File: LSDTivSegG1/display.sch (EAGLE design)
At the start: 99 parts, among them IC1 MEGA8-P, IC2 MAX232, IC3 PCF8574P, IC4 PCF8574P, IC5 PCF8574P, IC6 PCF8574P

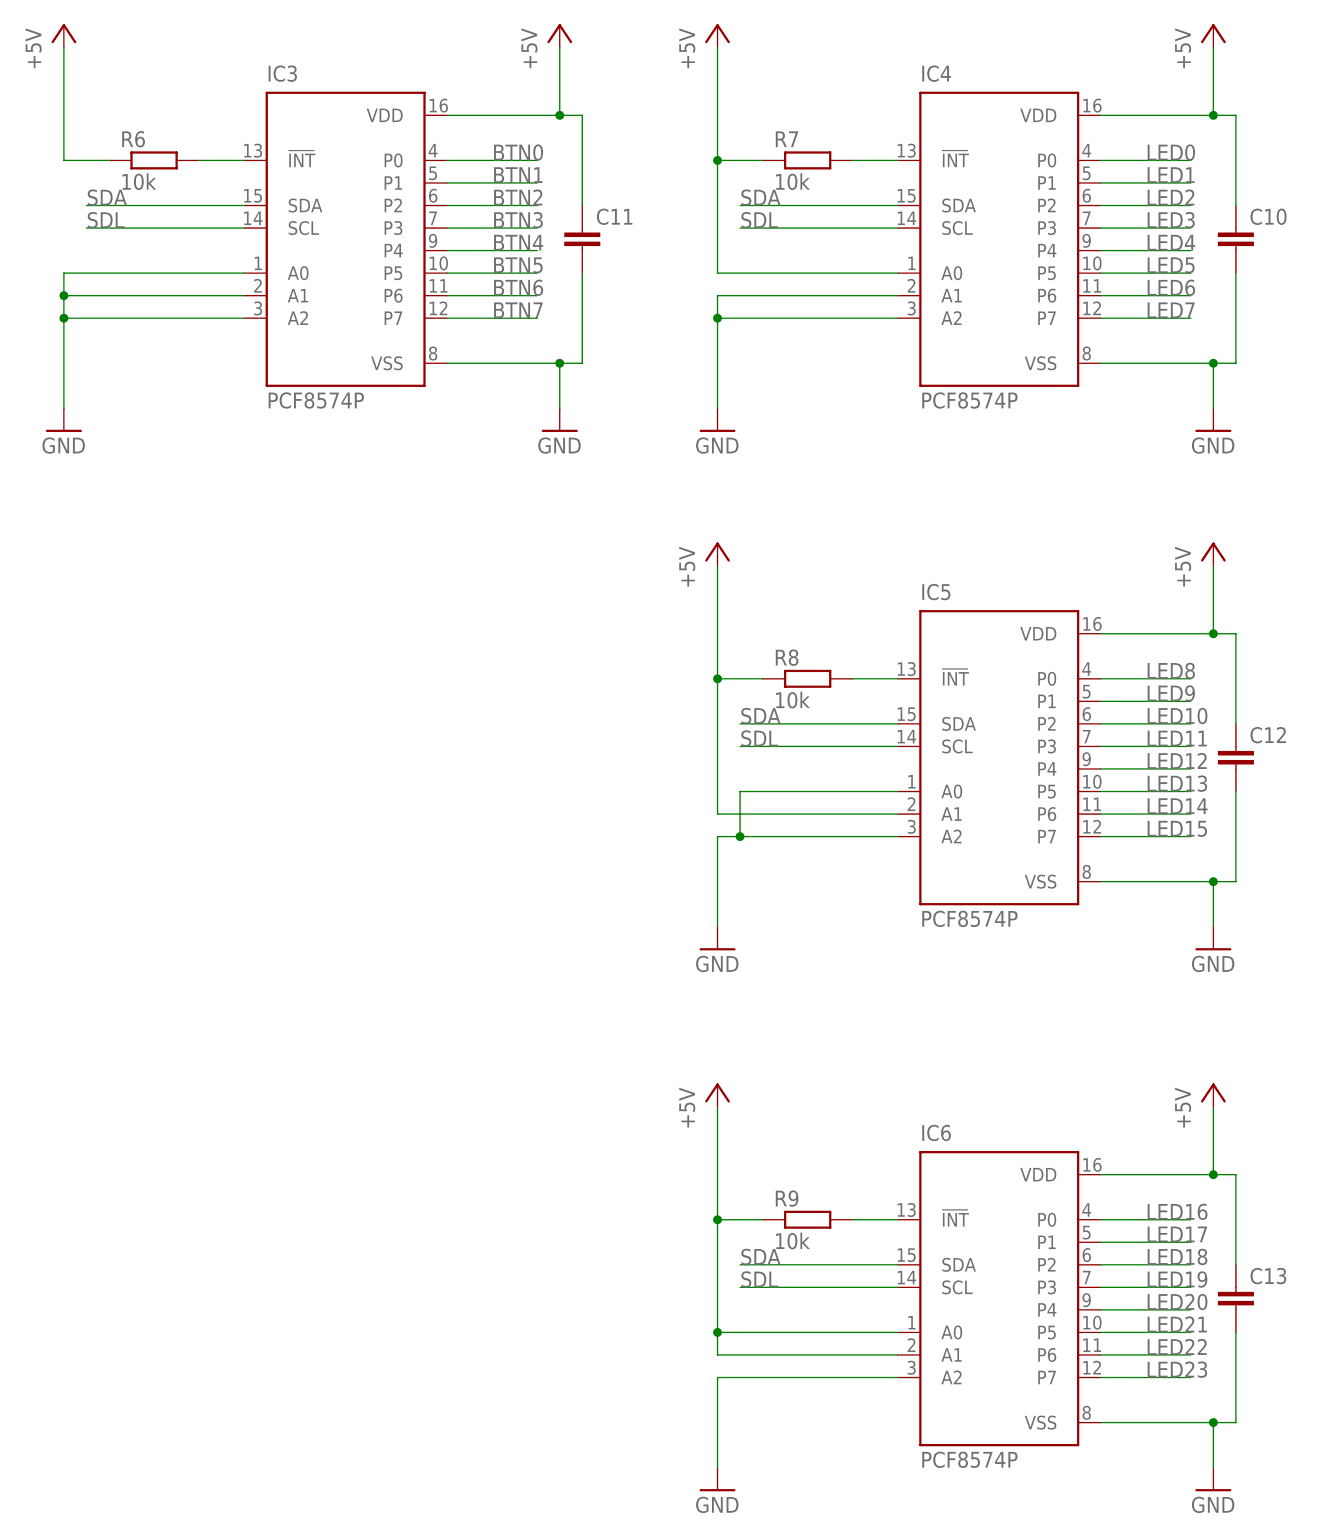
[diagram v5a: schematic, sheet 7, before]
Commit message: added values to PCF blocking capacities
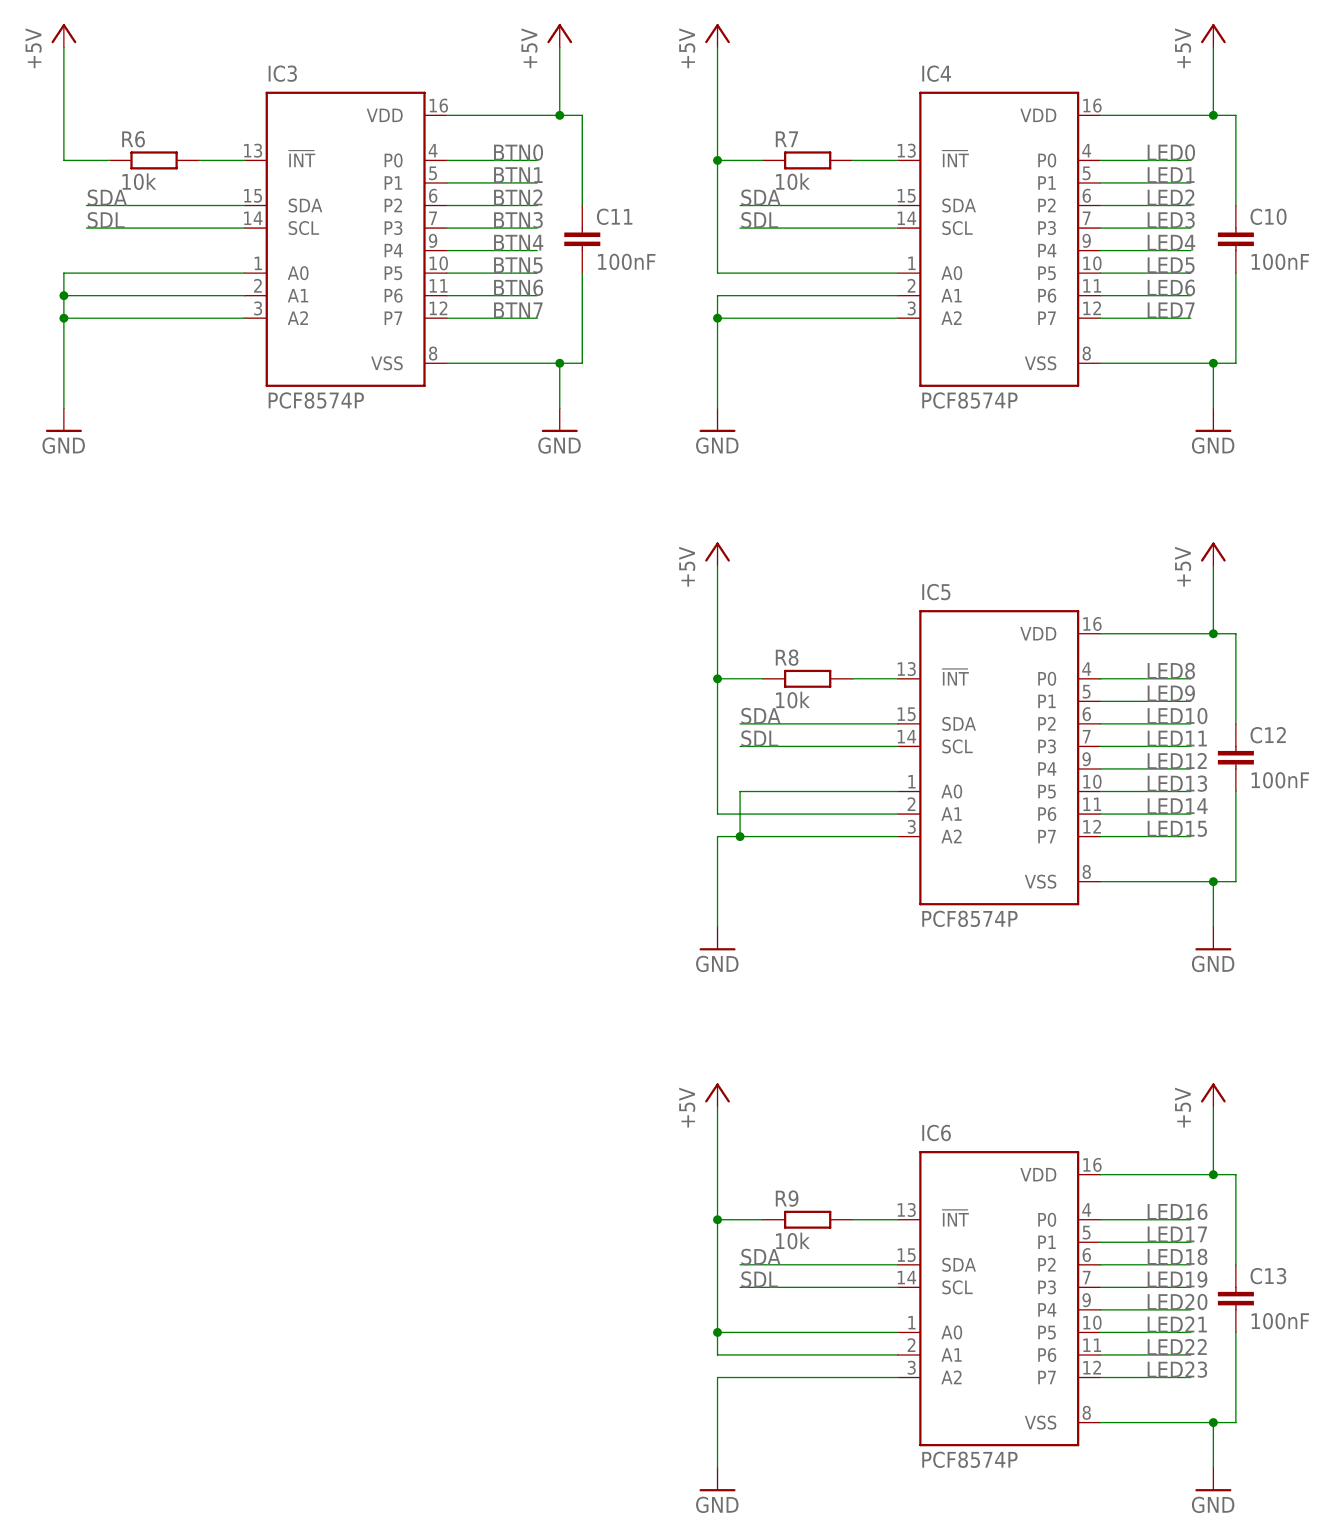
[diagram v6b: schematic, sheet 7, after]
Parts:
- C10, C11, C12, C13: value (none) -> 100nF
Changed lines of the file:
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@@
 <part name="JP1" library="pinhead" library_urn="urn:adsk.eagle:library:325" deviceset="PINHD-1X2" device="" package3d_urn="urn:adsk.eagle:package:22435/2"/>
 <part name="JP2" library="pinhead" library_urn="urn:adsk.eagle:library:325" deviceset="PINHD-2X3" device="" package3d_urn="urn:adsk.eagle:package:22462/2"/>
-<part name="C10" library="rcl" library_urn="urn:adsk.eagle:library:334" deviceset="C-EU" device="025-025X050" package3d_urn="urn:adsk.eagle:package:23629/2"/>
-<part name="C11" library="rcl" library_urn="urn:adsk.eagle:library:334" deviceset="C-EU" device="025-025X050" package3d_urn="urn:adsk.eagle:package:23629/2"/>
-<part name="C12" library="rcl" library_urn="urn:adsk.eagle:library:334" deviceset="C-EU" device="025-025X050" package3d_urn="urn:adsk.eagle:package:23629/2"/>
-<part name="C13" library="rcl" library_urn="urn:adsk.eagle:library:334" deviceset="C-EU" device="025-025X050" package3d_urn="urn:adsk.eagle:package:23629/2"/>
+<part name="C10" library="rcl" library_urn="urn:adsk.eagle:library:334" deviceset="C-EU" device="025-025X050" package3d_urn="urn:adsk.eagle:package:23629/2" value="100nF"/>
+<part name="C11" library="rcl" library_urn="urn:adsk.eagle:library:334" deviceset="C-EU" device="025-025X050" package3d_urn="urn:adsk.eagle:package:23629/2" value="100nF"/>
+<part name="C12" library="rcl" library_urn="urn:adsk.eagle:library:334" deviceset="C-EU" device="025-025X050" package3d_urn="urn:adsk.eagle:package:23629/2" value="100nF"/>
+<part name="C13" library="rcl" library_urn="urn:adsk.eagle:library:334" deviceset="C-EU" device="025-025X050" package3d_urn="urn:adsk.eagle:package:23629/2" value="100nF"/>
 <part name="R3" library="rcl" library_urn="urn:adsk.eagle:library:334" deviceset="R-EU_" device="0207/10" package3d_urn="urn:adsk.eagle:package:23491/1" value="15k"/>
 <part name="U$2" library="lsd2016" deviceset="DISPLAY_FRAME" device=""/>

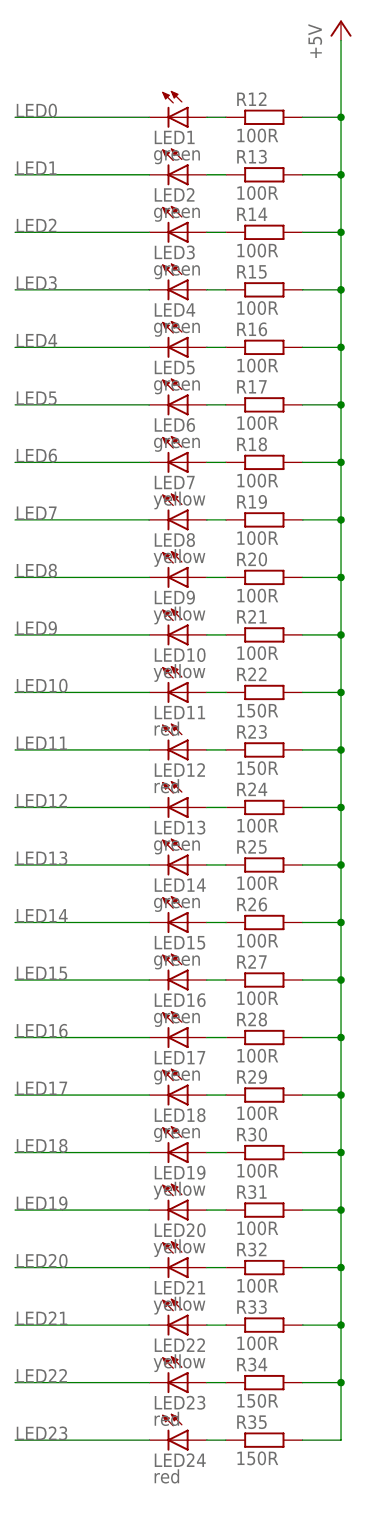
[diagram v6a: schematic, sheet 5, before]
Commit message: fixed some bugs in schematic board file with all components placed
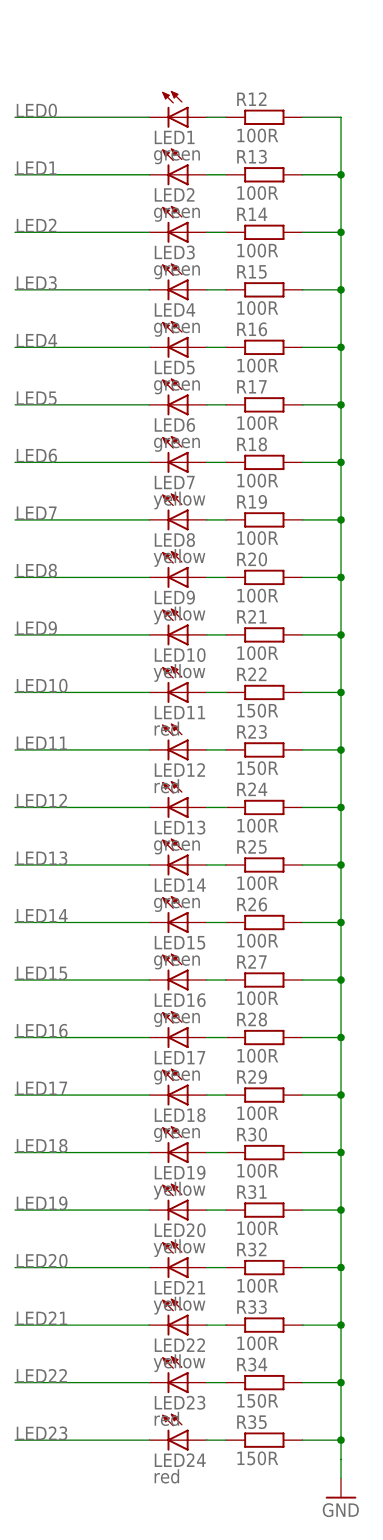
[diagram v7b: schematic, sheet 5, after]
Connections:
- net +5V: no longer R12.2, R13.2, R14.2, R15.2, R16.2, R17.2, R18.2, R19.2, R2.A, R20.2, R21.2, R22.2, R23.2, R24.2, R25.2, R26.2, R27.2, R28.2, R29.2, R30.2, R31.2, R32.2, R33.2, R34.2, R35.2, U$1.LED-, U$1.VSS
- net GND: now also R12.2, R13.2, R14.2, R15.2, R16.2, R17.2, R18.2, R19.2, R2.A, R20.2, R21.2, R22.2, R23.2, R24.2, R25.2, R26.2, R27.2, R28.2, R29.2, R30.2, R31.2, R32.2, R33.2, R34.2, R35.2, U$1.LED-, U$1.VSS

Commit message: worked on board layout (ca. 80% routed) changed LEDs from GND to +5V
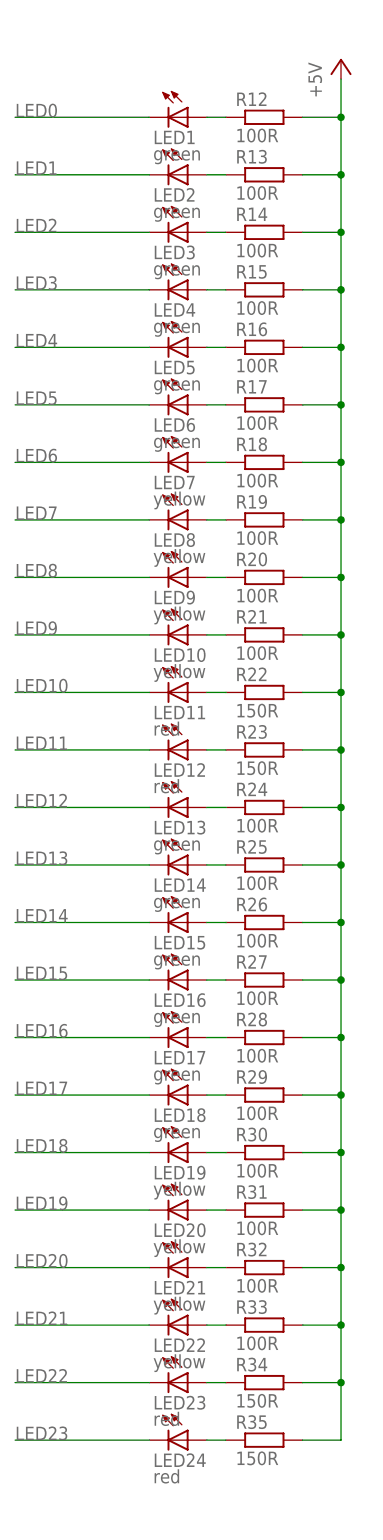
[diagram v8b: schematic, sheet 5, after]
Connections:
- net +5V: now also R12.2, R13.2, R14.2, R15.2, R16.2, R17.2, R18.2, R19.2, R20.2, R21.2, R22.2, R23.2, R24.2, R25.2, R26.2, R27.2, R28.2, R29.2, R30.2, R31.2, R32.2, R33.2, R34.2, R35.2
- net GND: no longer R12.2, R13.2, R14.2, R15.2, R16.2, R17.2, R18.2, R19.2, R20.2, R21.2, R22.2, R23.2, R24.2, R25.2, R26.2, R27.2, R28.2, R29.2, R30.2, R31.2, R32.2, R33.2, R34.2, R35.2
